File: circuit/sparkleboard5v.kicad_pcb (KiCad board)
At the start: 2 copper layers, 36.2 x 29.7 mm, 33 parts, among them J3 Conn_01x04_Pin, J4 Conn_01x02_Pin, J5 Conn_01x02_Pin, U6 AP63205WU

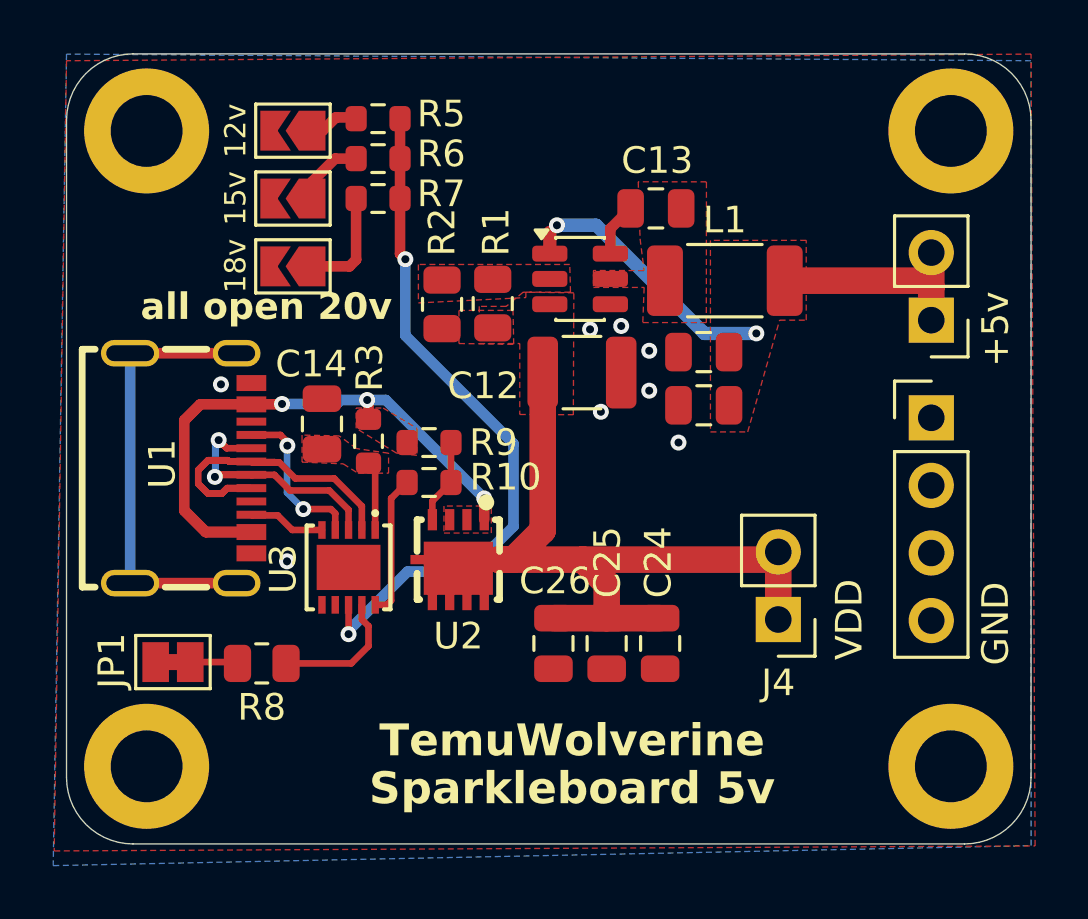
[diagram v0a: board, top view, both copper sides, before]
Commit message: tweaked spacing, updated readme
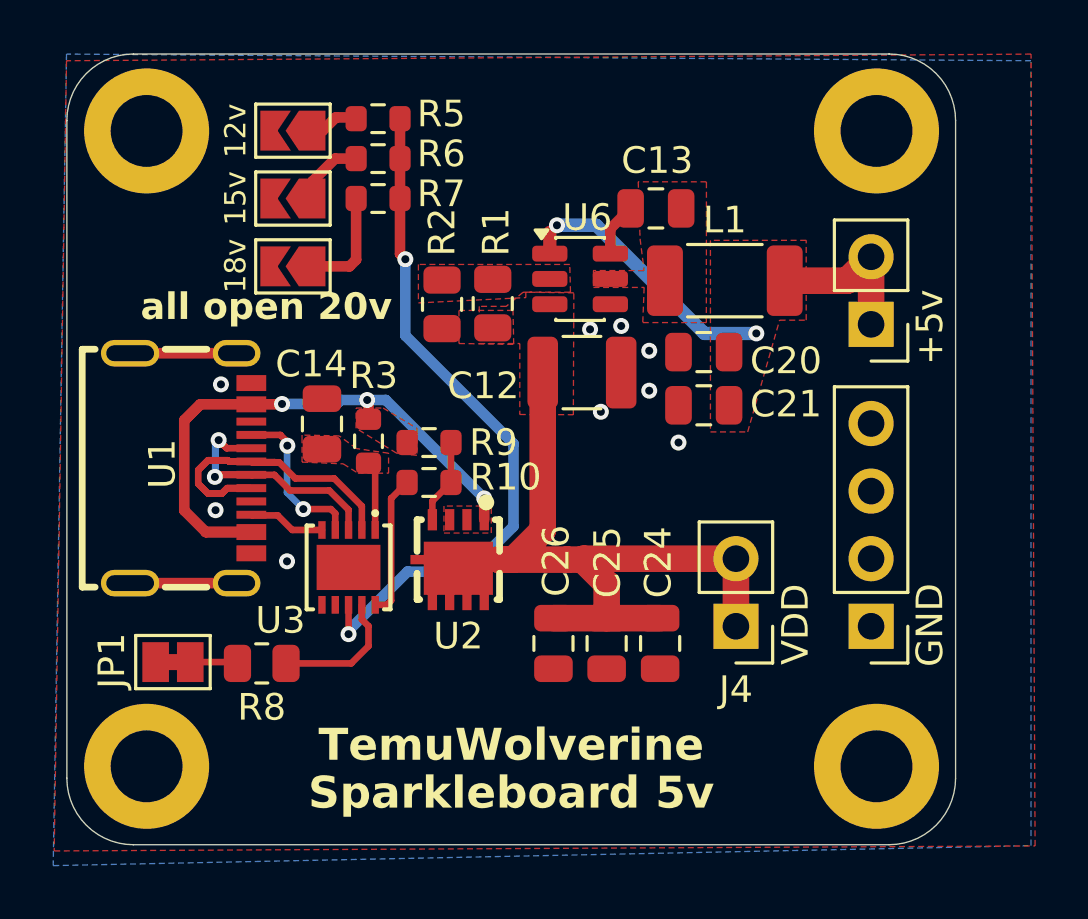
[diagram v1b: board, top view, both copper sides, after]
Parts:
- U1: value ~ -> C9900066641
- U2: value ~ -> AONR21307
- U3: value ~ -> HUSB238
- moved J3 8.15 mm to (122.4, 68.0), turned to 180 degrees
- moved H2 2.79 mm to (122.6, 49.4)
- moved H4 2.79 mm to (122.6, 73.3)
- moved J5 2.27 mm to (122.4, 56.6)
- moved J4 1.61 mm to (117.3, 68.0)
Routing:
- net unconnected-(U1-PadEH1): track 16.6 -> 8.00 mm
- net VDD: track 28.7 -> 26.4 mm
- net +5V: track 19.6 -> 17.6 mm
- net /VBUS: track 24.9 -> 23.8 mm
- net GND: vias 8 -> 9
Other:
- board size 36.2 x 29.7 mm -> 33.4 x 29.7 mm

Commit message: Updated board, added more plots for reddit review
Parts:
- removed JP1: Jumper_2_Bridged, Jumper:SolderJumper-2_P1.3mm_Bridged_Pad1.0x1.5mm
- added R4: 0, Resistor_SMD:R_0805_2012Metric, F.Cu at (101.8, 71.8)
- moved R8 2.33 mm to (101.8, 69.8)
- moved JP4 0.99 mm to (101.2, 53.6)
- moved JP3 0.99 mm to (101.2, 51.1)
- moved JP2 0.98 mm to (101.2, 48.5)
- moved R5 0.67 mm to (104.4, 48.5)
- moved R6 0.67 mm to (104.4, 50.0)
- moved R7 0.67 mm to (104.4, 51.5)
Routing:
- net VDD: track 26.4 -> 0.89 mm
- net +5V: track 17.6 -> 11.5 mm
- net Net-(JP3-A): track 2.64 -> 0.79 mm
- net /VBUS: track 23.8 -> 22.1 mm
- net ISET: track 5.02 -> 3.47 mm
- net Net-(JP2-A): track 1.88 -> 0.78 mm
- net Net-(JP4-A): track 4.05 -> 3.42 mm
- net GND: vias 9 -> 18
